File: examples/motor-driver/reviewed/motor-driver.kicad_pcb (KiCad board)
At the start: 2 copper layers, 88 x 50 mm, 12 parts, among them J1 VM 2.7-10.8V, J2 MOTOR A, J3 MOTOR B, J4 LOGIC, U1 DRV8833PW

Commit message: Arc out of a reversal at the line-out, and put the pour wedges back
Two corrections from review. The reversal now turns through every
intermediate 45 right where the line leaves the part - nine o'clock,
half-past ten, twelve, half-past one, three - by retracting along the
incoming leg and solving the arc onto the outgoing straight; the fold's
corners disappear instead of being spread, and the old three-millimetre
ride to the fan column goes with them. And the round-thirteen tongue
pruning is reverted: it was built on a misreading of the circles - the
pour filling a bent corner was never the complaint - so the fill goes
back to what the sweep makes of the copper.

Co-Authored-By: Claude Fable 5 <noreply@anthropic.com>
Claude-Session: https://claude.ai/code/session_01DUj7Ltu92tWg159mCSacwY
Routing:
- net /nFAULT: track 68.6 -> 65.3 mm
- net /nSLEEP: track 62.9 -> 59.6 mm
- net GND: vias 63 -> 65
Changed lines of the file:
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@@
 	(segment (start 141.1375 83.725) (end 137.5 83.725) (width 0.3) (layer "F.Cu") (net 15))
 	(segment (start 137.5 83.725) (end 134.875 81.1) (width 0.3) (layer "F.Cu") (net 15))
-	(segment (start 134.875 81.1) (end 132.6 81.1) (width 0.3) (layer "F.Cu") (net 15))
-	(segment (start 132.6 81.1) (end 132.0 80.5) (width 0.3) (layer "F.Cu") (net 15))
-	(segment (start 132.0 80.5) (end 132.0 79.9) (width 0.3) (layer "F.Cu") (net 15))
-	(segment (start 132.0 79.9) (end 133.4 78.5) (width 0.3) (layer "F.Cu") (net 15))
-	(segment (start 133.4 78.5) (end 134.5 78.5) (width 0.3) (layer "F.Cu") (net 15))
+	(segment (start 134.875 81.1) (end 134.575 81.1) (width 0.3) (layer "F.Cu") (net 15))
+	(segment (start 134.575 81.1) (end 133.7915 80.3165) (width 0.3) (layer "F.Cu") (net 15))
+	(segment (start 133.7915 80.3165) (end 133.7915 79.2085) (width 0.3) (layer "F.Cu") (net 15))
+	(segment (start 133.7915 79.2085) (end 134.5 78.5) (width 0.3) (layer "F.Cu") (net 15))
 	(segment (start 134.5 78.5) (end 173.75 78.5) (width 0.3) (layer "F.Cu") (net 15))
 	(segment (start 173.75 78.5) (end 176.75 81.5) (width 0.3) (layer "F.Cu") (net 15))
@@
 	(segment (start 141.1375 88.275) (end 137.5 88.275) (width 0.3) (layer "F.Cu") (net 14))
 	(segment (start 137.5 88.275) (end 134.875 90.9) (width 0.3) (layer "F.Cu") (net 14))
-	(segment (start 134.875 90.9) (end 132.6 90.9) (width 0.3) (layer "F.Cu") (net 14))
-	(segment (start 132.6 90.9) (end 132.0 91.5) (width 0.3) (layer "F.Cu") (net 14))
-	(segment (start 132.0 91.5) (end 132.0 92.1) (width 0.3) (layer "F.Cu") (net 14))
-	(segment (start 132.0 92.1) (end 141.4 101.5) (width 0.3) (layer "F.Cu") (net 14))
-	(segment (start 141.4 101.5) (end 142.5 101.5) (width 0.3) (layer "F.Cu") (net 14))
+	(segment (start 134.875 90.9) (end 134.575 90.9) (width 0.3) (layer "F.Cu") (net 14))
+	(segment (start 134.575 90.9) (end 133.7915 91.6835) (width 0.3) (layer "F.Cu") (net 14))
+	(segment (start 133.7915 91.6835) (end 133.7915 92.7915) (width 0.3) (layer "F.Cu") (net 14))
+	(segment (start 133.7915 92.7915) (end 142.5 101.5) (width 0.3) (layer "F.Cu") (net 14))
 	(segment (start 142.5 101.5) (end 166.375 101.5) (width 0.3) (layer "F.Cu") (net 14))
 	(segment (start 166.375 101.5) (end 167.0 100.875) (width 0.3) (layer "F.Cu") (net 14))
@@
 	(via (at 144.7 68.7) (size 0.8) (drill 0.4) (layers "F.Cu" "B.Cu") (net 1))
 	(via (at 120.7 80.7) (size 0.8) (drill 0.4) (layers "F.Cu" "B.Cu") (net 1))
+	(via (at 132.7 80.7) (size 0.8) (drill 0.4) (layers "F.Cu" "B.Cu") (net 1))
 	(via (at 144.7 80.7) (size 0.8) (drill 0.4) (layers "F.Cu" "B.Cu") (net 1))
 	(via (at 120.7 92.7) (size 0.8) (drill 0.4) (layers "F.Cu" "B.Cu") (net 1))
+	(via (at 132.7 92.7) (size 0.8) (drill 0.4) (layers "F.Cu" "B.Cu") (net 1))
 	(via (at 144.7 92.7) (size 0.8) (drill 0.4) (layers "F.Cu" "B.Cu") (net 1))
 	(via (at 156.7 92.7) (size 0.8) (drill 0.4) (layers "F.Cu" "B.Cu") (net 1))

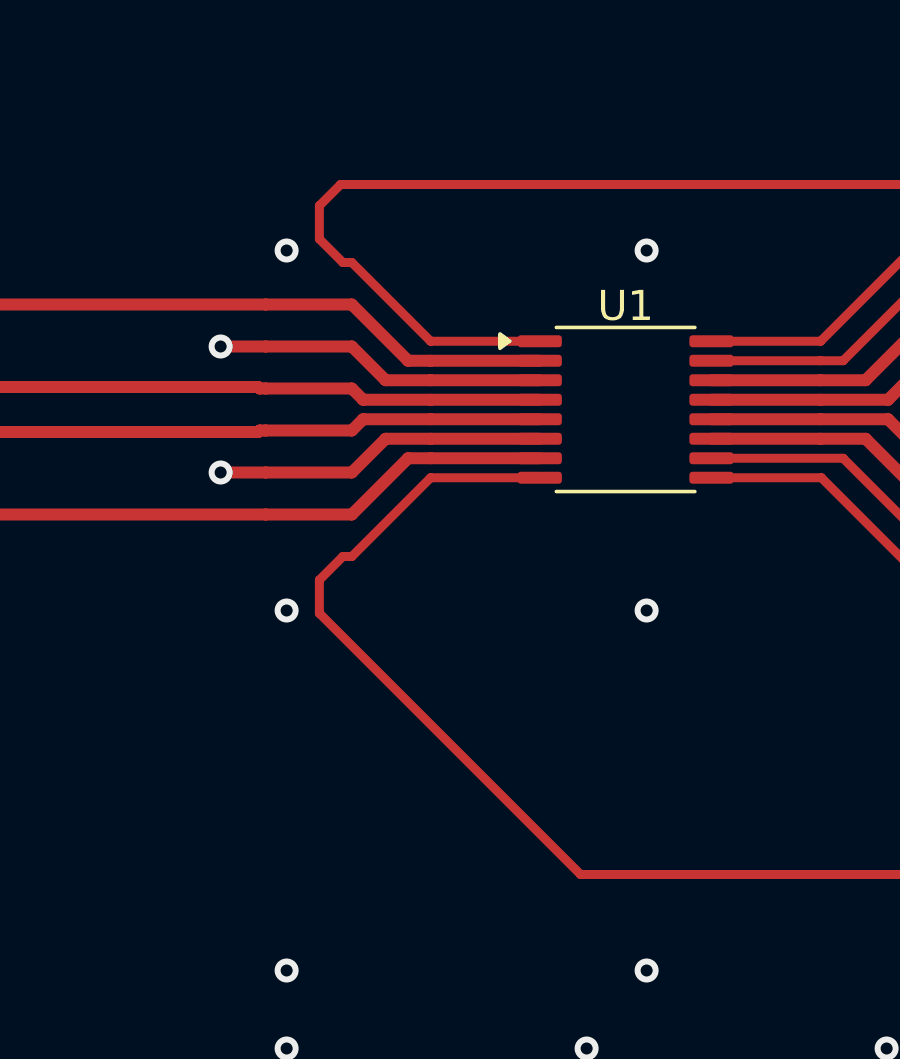
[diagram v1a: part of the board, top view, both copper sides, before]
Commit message: Stand the reversal up square at the line-out
The arc out of a fold gains one more correction from the reviewer: the
first 45 - half-past ten - made the turn read as an S. The intermediate
headings now start at 90 degrees, so the figure is the line-out, one
square stand-up, then half-past one and three, exactly as drawn.
Regenerate the motor board (the only one with such a fold) and rewrite
the REVIEW and guide passages that described the old shape.

Co-Authored-By: Claude Fable 5 <noreply@anthropic.com>
Claude-Session: https://claude.ai/code/session_01DUj7Ltu92tWg159mCSacwY
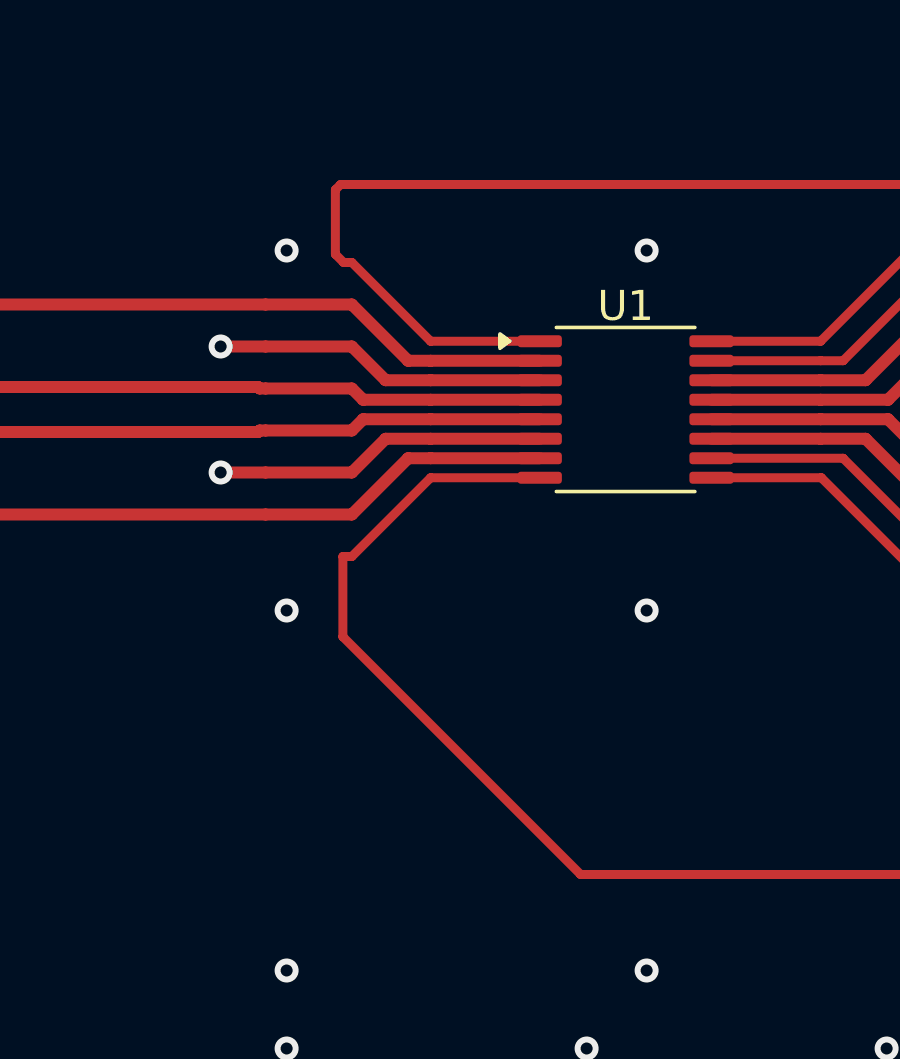
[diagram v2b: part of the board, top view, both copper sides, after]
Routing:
- net /nFAULT: track 65.3 -> 64.7 mm
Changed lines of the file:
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@@
 	(segment (start 141.1375 83.725) (end 137.5 83.725) (width 0.3) (layer "F.Cu") (net 15))
 	(segment (start 137.5 83.725) (end 134.875 81.1) (width 0.3) (layer "F.Cu") (net 15))
-	(segment (start 134.875 81.1) (end 134.575 81.1) (width 0.3) (layer "F.Cu") (net 15))
-	(segment (start 134.575 81.1) (end 133.7915 80.3165) (width 0.3) (layer "F.Cu") (net 15))
-	(segment (start 133.7915 80.3165) (end 133.7915 79.2085) (width 0.3) (layer "F.Cu") (net 15))
-	(segment (start 133.7915 79.2085) (end 134.5 78.5) (width 0.3) (layer "F.Cu") (net 15))
+	(segment (start 134.875 81.1) (end 134.6 81.1) (width 0.3) (layer "F.Cu") (net 15))
+	(segment (start 134.6 81.1) (end 134.325 80.825) (width 0.3) (layer "F.Cu") (net 15))
+	(segment (start 134.325 80.825) (end 134.325 78.675) (width 0.3) (layer "F.Cu") (net 15))
+	(segment (start 134.325 78.675) (end 134.5 78.5) (width 0.3) (layer "F.Cu") (net 15))
 	(segment (start 134.5 78.5) (end 173.75 78.5) (width 0.3) (layer "F.Cu") (net 15))
 	(segment (start 173.75 78.5) (end 176.75 81.5) (width 0.3) (layer "F.Cu") (net 15))
@@
 	(segment (start 137.5 88.275) (end 134.875 90.9) (width 0.3) (layer "F.Cu") (net 14))
 	(segment (start 134.875 90.9) (end 134.575 90.9) (width 0.3) (layer "F.Cu") (net 14))
-	(segment (start 134.575 90.9) (end 133.7915 91.6835) (width 0.3) (layer "F.Cu") (net 14))
-	(segment (start 133.7915 91.6835) (end 133.7915 92.7915) (width 0.3) (layer "F.Cu") (net 14))
-	(segment (start 133.7915 92.7915) (end 142.5 101.5) (width 0.3) (layer "F.Cu") (net 14))
+	(segment (start 134.575 90.9) (end 134.575 93.575) (width 0.3) (layer "F.Cu") (net 14))
+	(segment (start 134.575 93.575) (end 142.5 101.5) (width 0.3) (layer "F.Cu") (net 14))
 	(segment (start 142.5 101.5) (end 166.375 101.5) (width 0.3) (layer "F.Cu") (net 14))
 	(segment (start 166.375 101.5) (end 167.0 100.875) (width 0.3) (layer "F.Cu") (net 14))

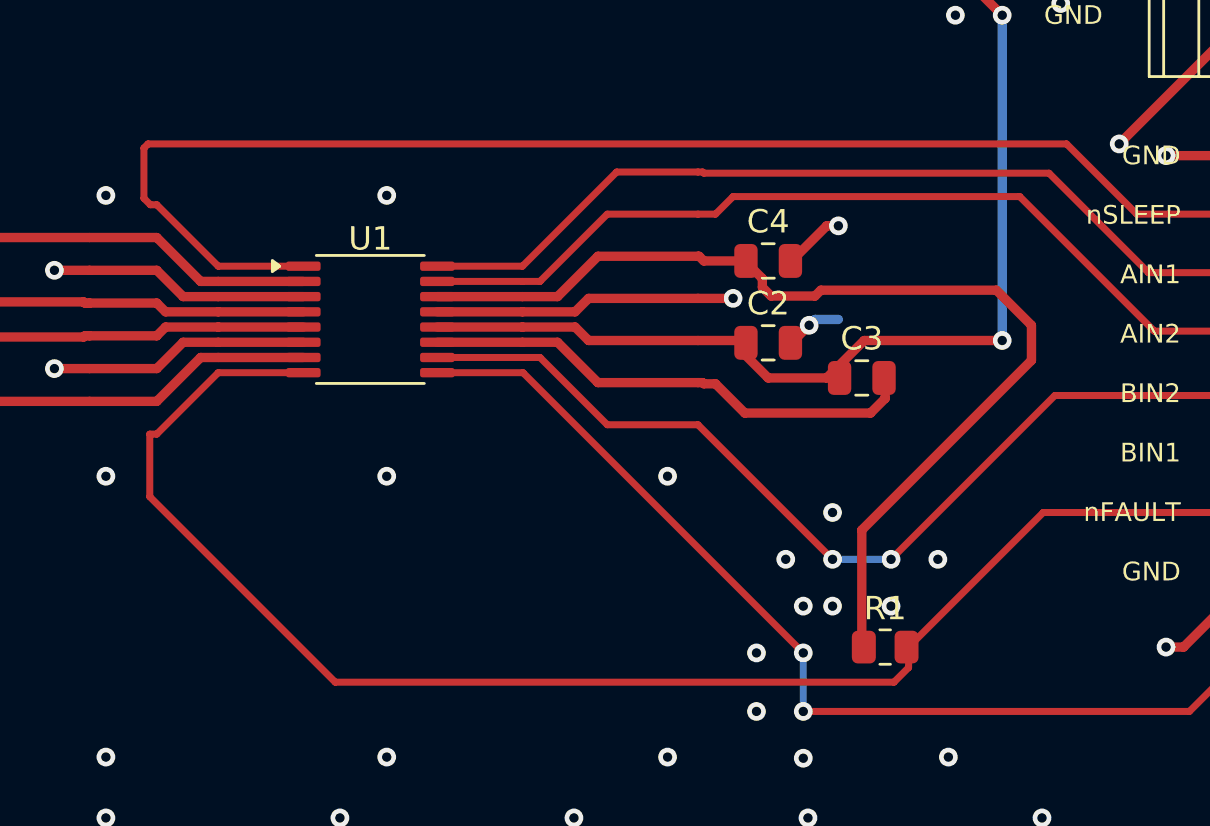
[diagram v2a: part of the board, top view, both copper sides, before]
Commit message: Start the turn at the head of the leg, with no stub at all
The reviewer's last correction on the reversal: the bend back to nine
o'clock - the lead stub the arc kept out the old heading - is not part
of the ideal figure. The turn now starts right where the incoming
straight begins, where the escape's own 45 already points the line, so
the trace draws one continuous curve from pad to bus. Two changes make
that fit: lead 0 is tried before any stub, and when the exit leg is too
short to land on without overshooting, the turn carries through the
exit's own 45 and lands on the straight beyond it.

The motor board's two reversals regenerate as equal-legged turns with
no stub; the FPGA board re-routes (the cache was lost to a container
reclaim) and reproduces its documented debt to the digit for a fourth
independent draw. The as-generated gate counts in the examples README
had drifted behind the rule set and are refreshed while the numbers
were being re-measured.

Co-Authored-By: Claude Fable 5 <noreply@anthropic.com>
Claude-Session: https://claude.ai/code/session_01DUj7Ltu92tWg159mCSacwY
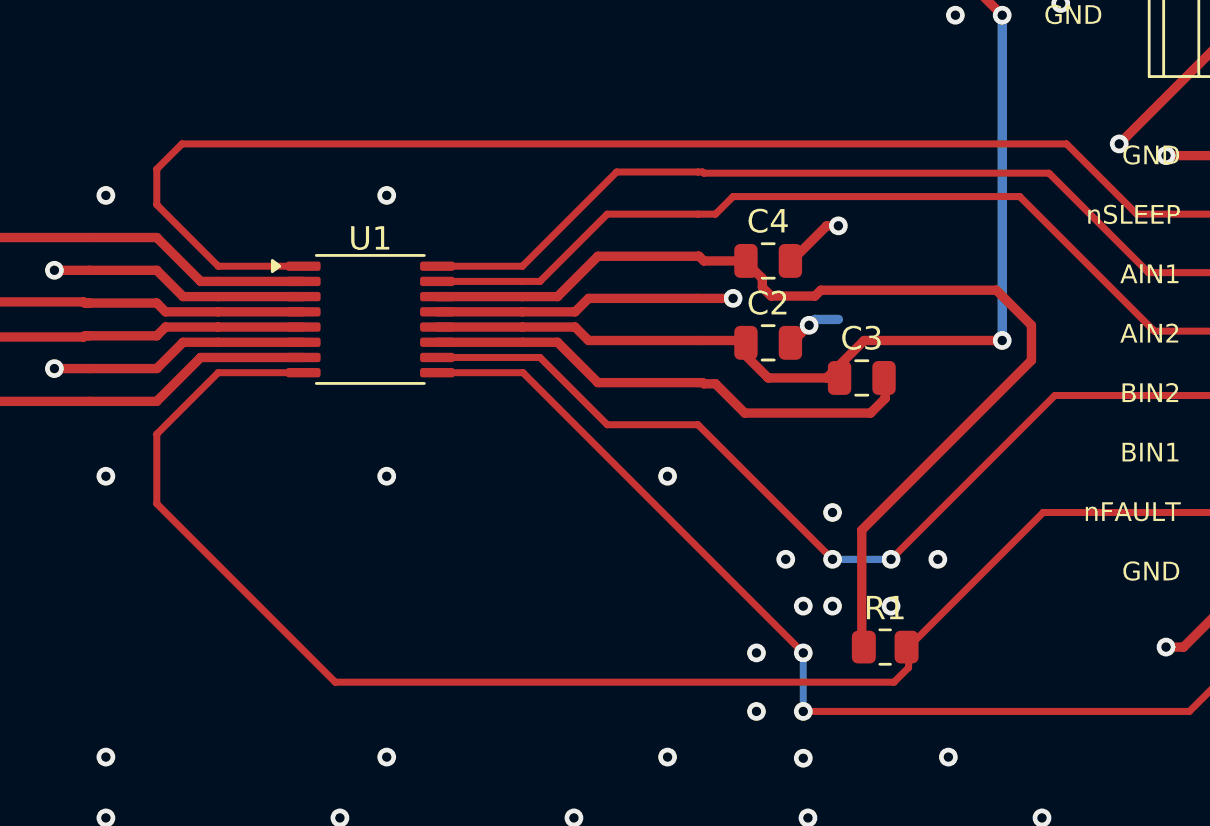
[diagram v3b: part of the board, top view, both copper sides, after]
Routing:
- net /nSLEEP: track 59.2 -> 57.7 mm
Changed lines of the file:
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@@
 	(segment (start 141.1375 83.725) (end 137.5 83.725) (width 0.3) (layer "F.Cu") (net 15))
 	(segment (start 137.5 83.725) (end 134.875 81.1) (width 0.3) (layer "F.Cu") (net 15))
-	(segment (start 134.875 81.1) (end 134.6 81.1) (width 0.3) (layer "F.Cu") (net 15))
-	(segment (start 134.6 81.1) (end 134.325 80.825) (width 0.3) (layer "F.Cu") (net 15))
-	(segment (start 134.325 80.825) (end 134.325 78.675) (width 0.3) (layer "F.Cu") (net 15))
-	(segment (start 134.325 78.675) (end 134.5 78.5) (width 0.3) (layer "F.Cu") (net 15))
-	(segment (start 134.5 78.5) (end 173.75 78.5) (width 0.3) (layer "F.Cu") (net 15))
+	(segment (start 134.875 81.1) (end 134.875 79.577) (width 0.3) (layer "F.Cu") (net 15))
+	(segment (start 134.875 79.577) (end 135.952 78.5) (width 0.3) (layer "F.Cu") (net 15))
+	(segment (start 135.952 78.5) (end 173.75 78.5) (width 0.3) (layer "F.Cu") (net 15))
 	(segment (start 173.75 78.5) (end 176.75 81.5) (width 0.3) (layer "F.Cu") (net 15))
 	(segment (start 176.75 81.5) (end 181.75 81.5) (width 0.3) (layer "F.Cu") (net 15))
@@
 	(segment (start 141.1375 88.275) (end 137.5 88.275) (width 0.3) (layer "F.Cu") (net 14))
 	(segment (start 137.5 88.275) (end 134.875 90.9) (width 0.3) (layer "F.Cu") (net 14))
-	(segment (start 134.875 90.9) (end 134.575 90.9) (width 0.3) (layer "F.Cu") (net 14))
-	(segment (start 134.575 90.9) (end 134.575 93.575) (width 0.3) (layer "F.Cu") (net 14))
-	(segment (start 134.575 93.575) (end 142.5 101.5) (width 0.3) (layer "F.Cu") (net 14))
+	(segment (start 134.875 90.9) (end 134.875 93.875) (width 0.3) (layer "F.Cu") (net 14))
+	(segment (start 134.875 93.875) (end 142.5 101.5) (width 0.3) (layer "F.Cu") (net 14))
 	(segment (start 142.5 101.5) (end 166.375 101.5) (width 0.3) (layer "F.Cu") (net 14))
 	(segment (start 166.375 101.5) (end 167.0 100.875) (width 0.3) (layer "F.Cu") (net 14))
